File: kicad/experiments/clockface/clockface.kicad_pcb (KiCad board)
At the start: 2 copper layers, 50 x 50 mm, 11 parts, among them P1 CONN_01X05, U1 TOUCH_PAD_13, U2 MTCH6102_SSOP

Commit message: Pin 1 marker
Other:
- board text added: "."
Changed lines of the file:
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@@
-(kicad_pcb (version 4) (host pcbnew 4.0.2-4+6225~38~ubuntu14.04.1-stable)
+(kicad_pcb (version 4) (host pcbnew 4.0.2-stable)
   (general
     (links 40)
     (no_connects 0)
-    (area 122.741999 67.691 172.892001 120.021)
+    (area 122.741999 68.527999 172.892001 118.678001)
     (thickness 1.6)
-    (drawings 26)
+    (drawings 28)
     (tracks 241)
     (zones 0)
@@
   (page A4)
   (layers
-    (0 F.Cu signal)
+    (0 F.Cu signal hide)
     (31 B.Cu signal)
     (32 B.Adhes user)
@@
     (aux_axis_origin 0 0)
     (grid_origin 147.86864 93.93174)
-    (visible_elements 7FFFF7FF)
+    (visible_elements 7FFFF5FF)
     (pcbplotparams
       (layerselection 0x010f0_80000001)
@@
     )
   )
+  (gr_text . (at 146.09064 96.97974) (layer B.Mask)
+    (effects (font (size 3 3) (thickness 0.3)) (justify mirror))
+  )
+  (gr_text . (at 144.05864 98.50374) (layer B.Mask)
+    (effects (font (size 1.5 1.5) (thickness 0.3)) (justify mirror))
+  )
   (gr_circle (center 147.86864 93.93174) (end 139.99464 85.80374) (layer Cmts.User) (width 0.2))

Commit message: Corrected SDA & SCL labels
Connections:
- P1 pad 2: /SCL -> /SDA
- P1 pad 3: /SDA -> /SCL
- R3 pad 2: /SDA -> /SCL
- R4 pad 2: /SCL -> /SDA
- U2 pad 14: /SDA -> /SCL
- U2 pad 15: /SCL -> /SDA
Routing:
- net /SDA: track 30.7 -> 34.5 mm
- net /SCL: track 34.5 -> 30.7 mm
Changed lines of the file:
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@@
     (links 40)
     (no_connects 0)
-    (area 122.741999 68.527999 172.892001 118.678001)
+    (area 122.741999 67.691 172.892001 120.021)
     (thickness 1.6)
     (drawings 28)
@@
       (layerselection 0x010f0_80000001)
       (usegerberextensions true)
-      (usegerberattributes true)
       (excludeedgelayer true)
       (linewidth 0.100000)
@@
       (net 26 /3V3))
     (pad 2 smd rect (at 1.35 0 180) (size 1.5 1.3) (layers B.Cu B.Paste B.Mask)
-      (net 4 /SDA))
+      (net 5 /SCL))
     (model Resistors_SMD.3dshapes/R_0805_HandSoldering.wrl
       (at (xyz 0 0 0))
@@
       (net 26 /3V3))
     (pad 2 smd rect (at 1.35 0 180) (size 1.5 1.3) (layers B.Cu B.Paste B.Mask)
-      (net 5 /SCL))
+      (net 4 /SDA))
     (model Resistors_SMD.3dshapes/R_0805_HandSoldering.wrl
       (at (xyz 0 0 0))
@@
       (net 26 /3V3))
     (pad 2 connect oval (at 1.016 -2.54 90) (size 4.064 1.7272) (layers B.Cu B.Mask)
+      (net 4 /SDA))
+    (pad 3 connect oval (at 1.016 -5.08 90) (size 4.064 1.7272) (layers B.Cu B.Mask)
       (net 5 /SCL))
-    (pad 3 connect oval (at 1.016 -5.08 90) (size 4.064 1.7272) (layers B.Cu B.Mask)
-      (net 4 /SDA))
     (pad 4 connect oval (at 1.016 -7.62 90) (size 4.064 1.7272) (layers B.Cu B.Mask)
       (net 6 /INT))
@@
       (net 1 GND) (solder_mask_margin 0.0508))
     (pad 14 smd rect (at -3.6 -4.225) (size 1.75 0.45) (layers B.Cu B.Paste B.Mask)
+      (net 5 /SCL) (solder_mask_margin 0.0508))
+    (pad 15 smd rect (at 3.6 -4.225) (size 1.75 0.45) (layers B.Cu B.Paste B.Mask)
       (net 4 /SDA) (solder_mask_margin 0.0508))
-    (pad 15 smd rect (at 3.6 -4.225) (size 1.75 0.45) (layers B.Cu B.Paste B.Mask)
-      (net 5 /SCL) (solder_mask_margin 0.0508))
     (pad 16 smd rect (at 3.6 -3.575) (size 1.75 0.45) (layers B.Cu B.Paste B.Mask)
       (net 19 /RX0) (solder_mask_margin 0.0508))
@@
     (effects (font (size 1 1) (thickness 0.15)) (justify mirror))
   )
-  (gr_text SDA (at 132.62864 75.89774 33) (layer B.SilkS)
+  (gr_text SDA (at 134.91464 75.89774 33) (layer B.SilkS)
     (effects (font (size 1 1) (thickness 0.15)) (justify mirror))
   )
-  (gr_text SCL (at 134.91464 75.89774 33) (layer B.SilkS)
+  (gr_text SCL (at 132.50164 75.89774 33) (layer B.SilkS)
     (effects (font (size 1 1) (thickness 0.15)) (justify mirror))
   )
@@
   (segment (start 146.39164 98.93174) (end 146.39164 100.78974) (width 0.305) (layer B.Cu) (net 3))
   (segment (start 145.5379 98.078) (end 146.39164 98.93174) (width 0.305) (layer B.Cu) (net 3))
-  (segment (start 146.51864 86.31174) (end 145.20164 86.31174) (width 0.305) (layer B.Cu) (net 4))
-  (segment (start 132.62864 75.64374) (end 132.62864 73.61174) (width 0.305) (layer B.Cu) (net 4))
-  (segment (start 133.39064 76.40574) (end 132.62864 75.64374) (width 0.305) (layer B.Cu) (net 4))
-  (segment (start 143.80464 76.40574) (end 133.39064 76.40574) (width 0.305) (layer B.Cu) (net 4))
-  (segment (start 144.82064 77.42174) (end 143.80464 76.40574) (width 0.305) (layer B.Cu) (net 4))
-  (segment (start 144.82064 85.93074) (end 144.82064 77.42174) (width 0.305) (layer B.Cu) (net 4))
-  (segment (start 145.20164 86.31174) (end 144.82064 85.93074) (width 0.305) (layer B.Cu) (net 4))
-  (segment (start 144.101 89.628) (end 145.82238 89.628) (width 0.305) (layer B.Cu) (net 4))
-  (segment (start 146.51864 88.93174) (end 146.51864 86.31174) (width 0.305) (layer B.Cu) (net 4))
-  (segment (start 145.82238 89.628) (end 146.51864 88.93174) (width 0.305) (layer B.Cu) (net 4))
-  (segment (start 146.51864 83.51774) (end 147.61464 83.51774) (width 0.305) (layer B.Cu) (net 5))
-  (segment (start 151.301 82.3781) (end 151.301 89.628) (width 0.305) (layer B.Cu) (net 5))
-  (segment (start 150.66264 81.73974) (end 151.301 82.3781) (width 0.305) (layer B.Cu) (net 5))
-  (segment (start 148.24964 81.73974) (end 150.66264 81.73974) (width 0.305) (layer B.Cu) (net 5))
-  (segment (start 147.86864 82.12074) (end 148.24964 81.73974) (width 0.305) (layer B.Cu) (net 5))
-  (segment (start 147.86864 83.26374) (end 147.86864 82.12074) (width 0.305) (layer B.Cu) (net 5))
-  (segment (start 147.61464 83.51774) (end 147.86864 83.26374) (width 0.305) (layer B.Cu) (net 5))
-  (segment (start 146.51864 83.51774) (end 146.51864 78.13674) (width 0.305) (layer B.Cu) (net 5))
-  (segment (start 135.16864 75.13574) (end 135.16864 73.61174) (width 0.305) (layer B.Cu) (net 5))
-  (segment (start 135.80364 75.77074) (end 135.16864 75.13574) (width 0.305) (layer B.Cu) (net 5))
-  (segment (start 144.15264 75.77074) (end 135.80364 75.77074) (width 0.305) (layer B.Cu) (net 5))
-  (segment (start 146.51864 78.13674) (end 144.15264 75.77074) (width 0.305) (layer B.Cu) (net 5))
-  (segment (start 146.51864 82.20074) (end 146.51864 83.51774) (width 0.305) (layer B.Cu) (net 5))
+  (segment (start 146.51864 83.51774) (end 147.61464 83.51774) (width 0.305) (layer B.Cu) (net 4))
+  (segment (start 151.301 82.3781) (end 151.301 89.628) (width 0.305) (layer B.Cu) (net 4))
+  (segment (start 150.66264 81.73974) (end 151.301 82.3781) (width 0.305) (layer B.Cu) (net 4))
+  (segment (start 148.24964 81.73974) (end 150.66264 81.73974) (width 0.305) (layer B.Cu) (net 4))
+  (segment (start 147.86864 82.12074) (end 148.24964 81.73974) (width 0.305) (layer B.Cu) (net 4))
+  (segment (start 147.86864 83.26374) (end 147.86864 82.12074) (width 0.305) (layer B.Cu) (net 4))
+  (segment (start 147.61464 83.51774) (end 147.86864 83.26374) (width 0.305) (layer B.Cu) (net 4))
+  (segment (start 146.51864 83.51774) (end 146.51864 78.13674) (width 0.305) (layer B.Cu) (net 4))
+  (segment (start 146.51864 78.13674) (end 144.15264 75.77074) (width 0.305) (layer B.Cu) (net 4))
+  (segment (start 146.51864 82.20074) (end 146.51864 83.51774) (width 0.305) (layer B.Cu) (net 4))
+  (segment (start 135.16864 75.13574) (end 135.16864 73.61174) (width 0.305) (layer B.Cu) (net 4))
+  (segment (start 135.80364 75.77074) (end 135.16864 75.13574) (width 0.305) (layer B.Cu) (net 4))
+  (segment (start 144.15264 75.77074) (end 135.80364 75.77074) (width 0.305) (layer B.Cu) (net 4))
+  (segment (start 132.62864 75.64374) (end 132.62864 73.61174) (width 0.305) (layer B.Cu) (net 5))
+  (segment (start 133.39064 76.40574) (end 132.62864 75.64374) (width 0.305) (layer B.Cu) (net 5))
+  (segment (start 143.80464 76.40574) (end 133.39064 76.40574) (width 0.305) (layer B.Cu) (net 5))
+  (segment (start 144.82064 77.42174) (end 143.80464 76.40574) (width 0.305) (layer B.Cu) (net 5))
+  (segment (start 144.82064 85.93074) (end 144.82064 77.42174) (width 0.305) (layer B.Cu) (net 5))
+  (segment (start 146.51864 86.31174) (end 145.20164 86.31174) (width 0.305) (layer B.Cu) (net 5))
+  (segment (start 145.20164 86.31174) (end 144.82064 85.93074) (width 0.305) (layer B.Cu) (net 5))
+  (segment (start 144.101 89.628) (end 145.82238 89.628) (width 0.305) (layer B.Cu) (net 5))
+  (segment (start 146.51864 88.93174) (end 146.51864 86.31174) (width 0.305) (layer B.Cu) (net 5))
+  (segment (start 145.82238 89.628) (end 146.51864 88.93174) (width 0.305) (layer B.Cu) (net 5))
   (segment (start 130.08864 73.61174) (end 130.08864 75.51674) (width 0.305) (layer B.Cu) (net 6))
   (segment (start 141.7049 91.578) (end 144.101 91.578) (width 0.305) (layer B.Cu) (net 6))

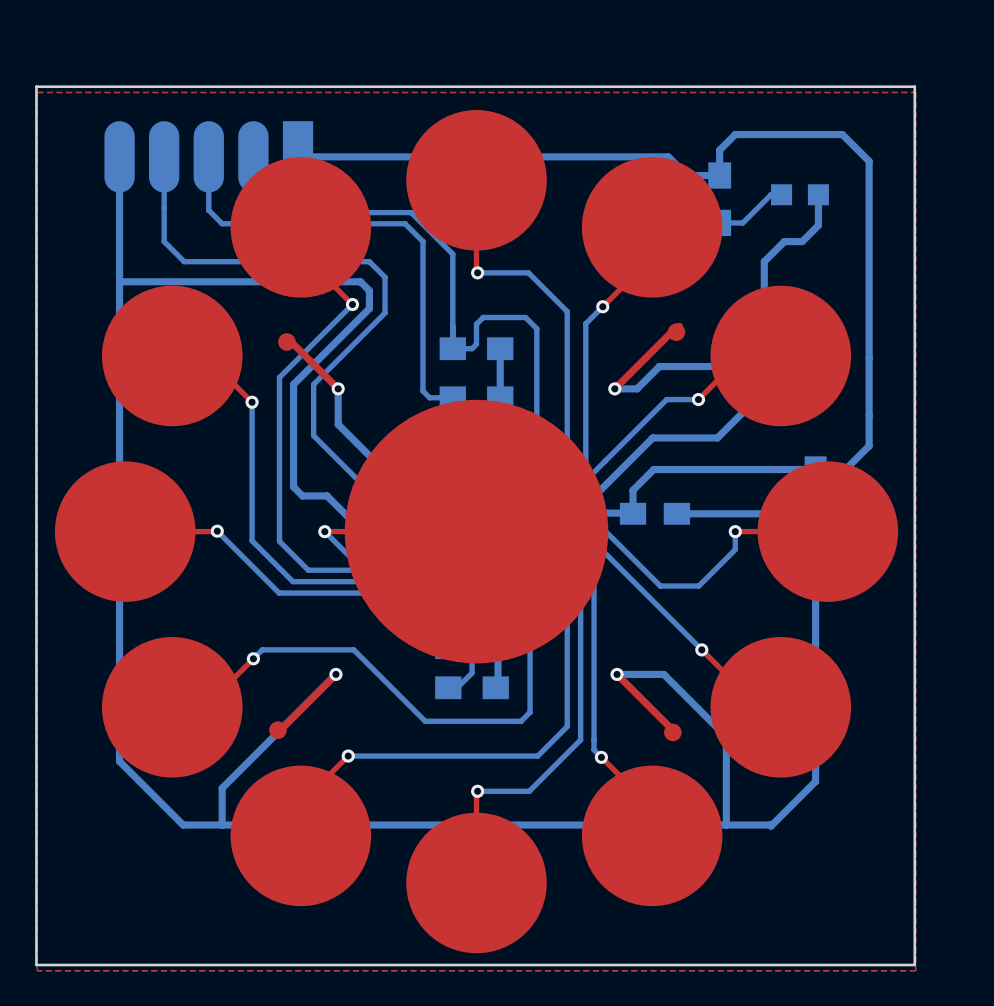
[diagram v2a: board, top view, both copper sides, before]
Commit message: Flip layers
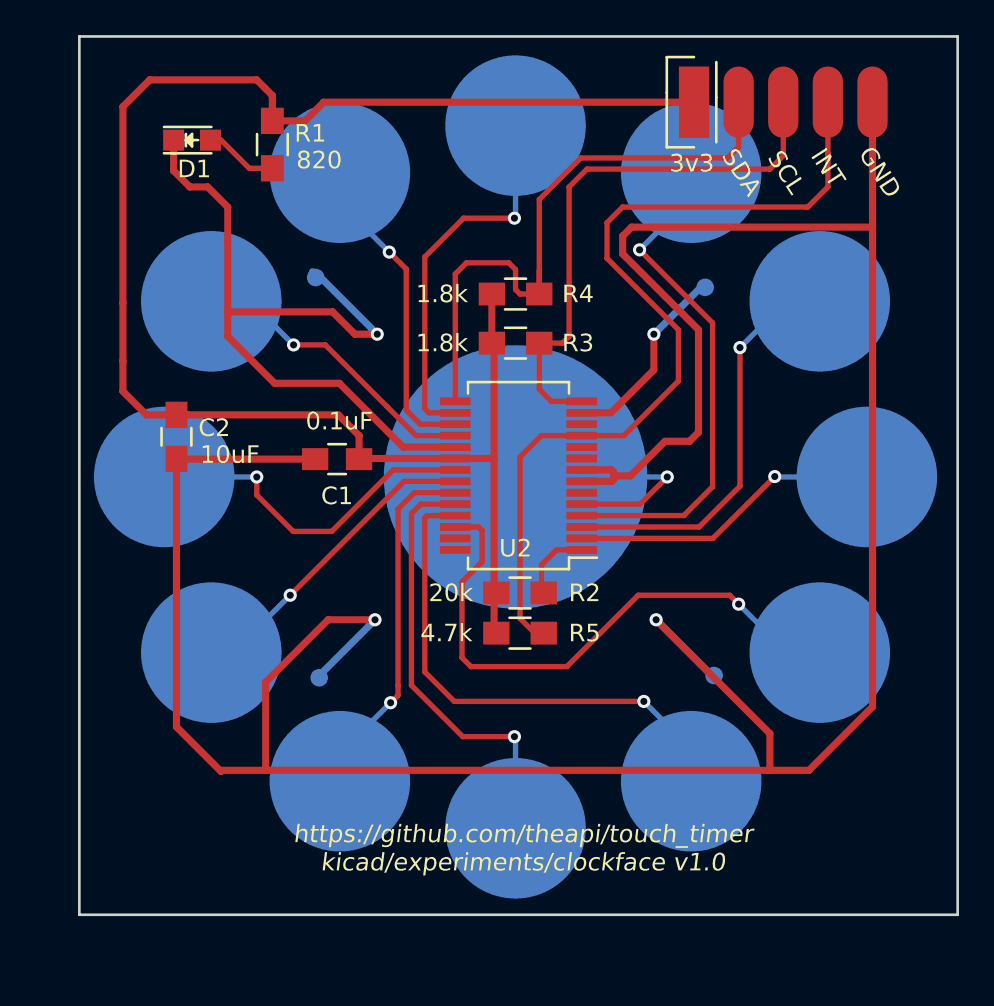
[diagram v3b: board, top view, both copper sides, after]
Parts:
- C1, C2, D1, P1, R1, R2, R3, R4, R5, U2: moved to F.Cu
- U1: moved to B.Cu
- moved C2 36.5 mm to (130.8, 88.5)
- moved D1 34.7 mm to (131.7, 71.6), turned to 0 degrees
- moved R1 25.7 mm to (136.2, 71.9)
- moved P1 22.8 mm to (160.3, 70.5)
- moved C1 18.4 mm to (139.9, 89.8), turned to 180 degrees
- moved R2 4.14 mm to (150.3, 97.4), turned to 0 degrees
- moved R5 4.14 mm to (150.3, 99.7), turned to 0 degrees
- moved U2 4.03 mm to (150.3, 90.7), turned to 180 degrees
- moved R3 3.82 mm to (150.1, 83.2), turned to 0 degrees
- moved R4 3.82 mm to (150.1, 80.4), turned to 0 degrees
- moved U1 3.82 mm to (150.1, 90.8), turned to 180 degrees
